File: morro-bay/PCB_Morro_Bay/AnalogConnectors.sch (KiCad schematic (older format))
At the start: 32 parts, among them J10 Conn_01x04, J11 Conn_01x04, J12 Conn_01x04, J13 Conn_01x04, J14 Conn_01x04, J15 Conn_01x04, J16 Conn_01x04, J17 Conn_01x04, J18 Conn_01x04, J19 Conn_01x04, J20 Conn_01x04, J21 Conn_01x04, J22 Conn_01x04, J24 Conn_01x04, J25 Conn_01x04, J26 Conn_01x04, J27 Conn_01x04, J28 Conn_01x04, J29 Conn_01x04, J3 Conn_01x04, J30 Conn_01x04, J31 Conn_01x04, J32 Conn_01x04, J33 Conn_01x04, J34 Conn_01x04, J35 Conn_01x04, J4 Conn_01x04, J5 Conn_01x04, J6 Conn_01x04, J7 Conn_01x04, J8 Conn_01x04, J9 Conn_01x04

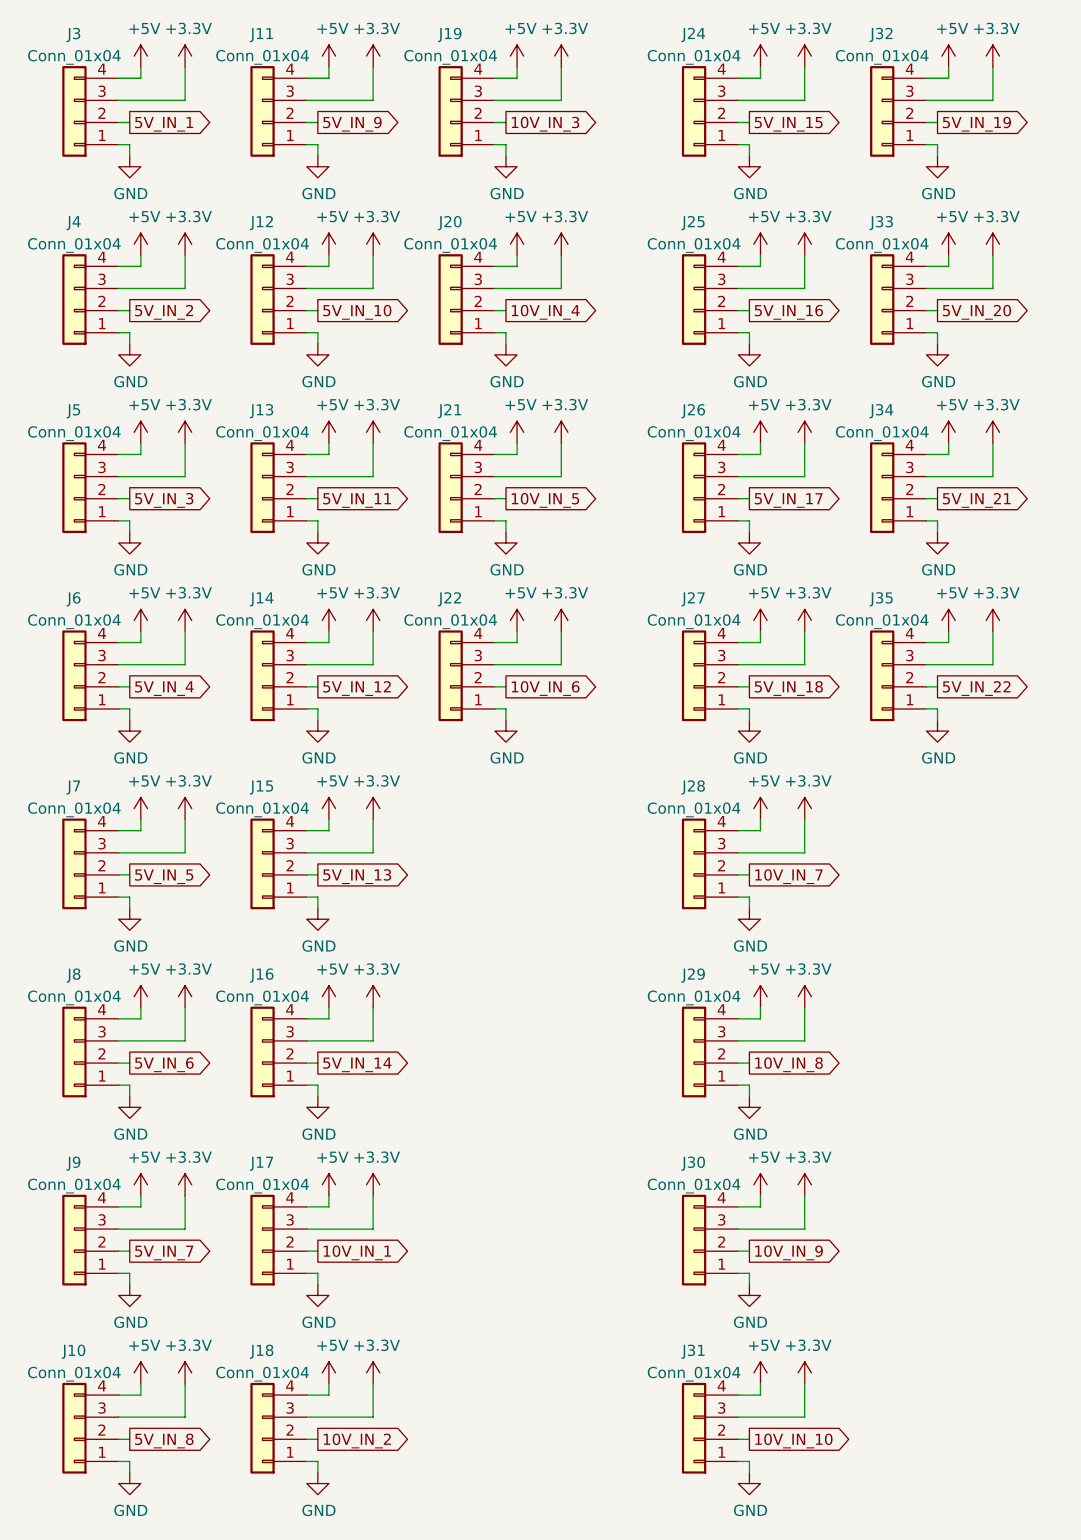
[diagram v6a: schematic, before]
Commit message: Fix values of C7 and C8
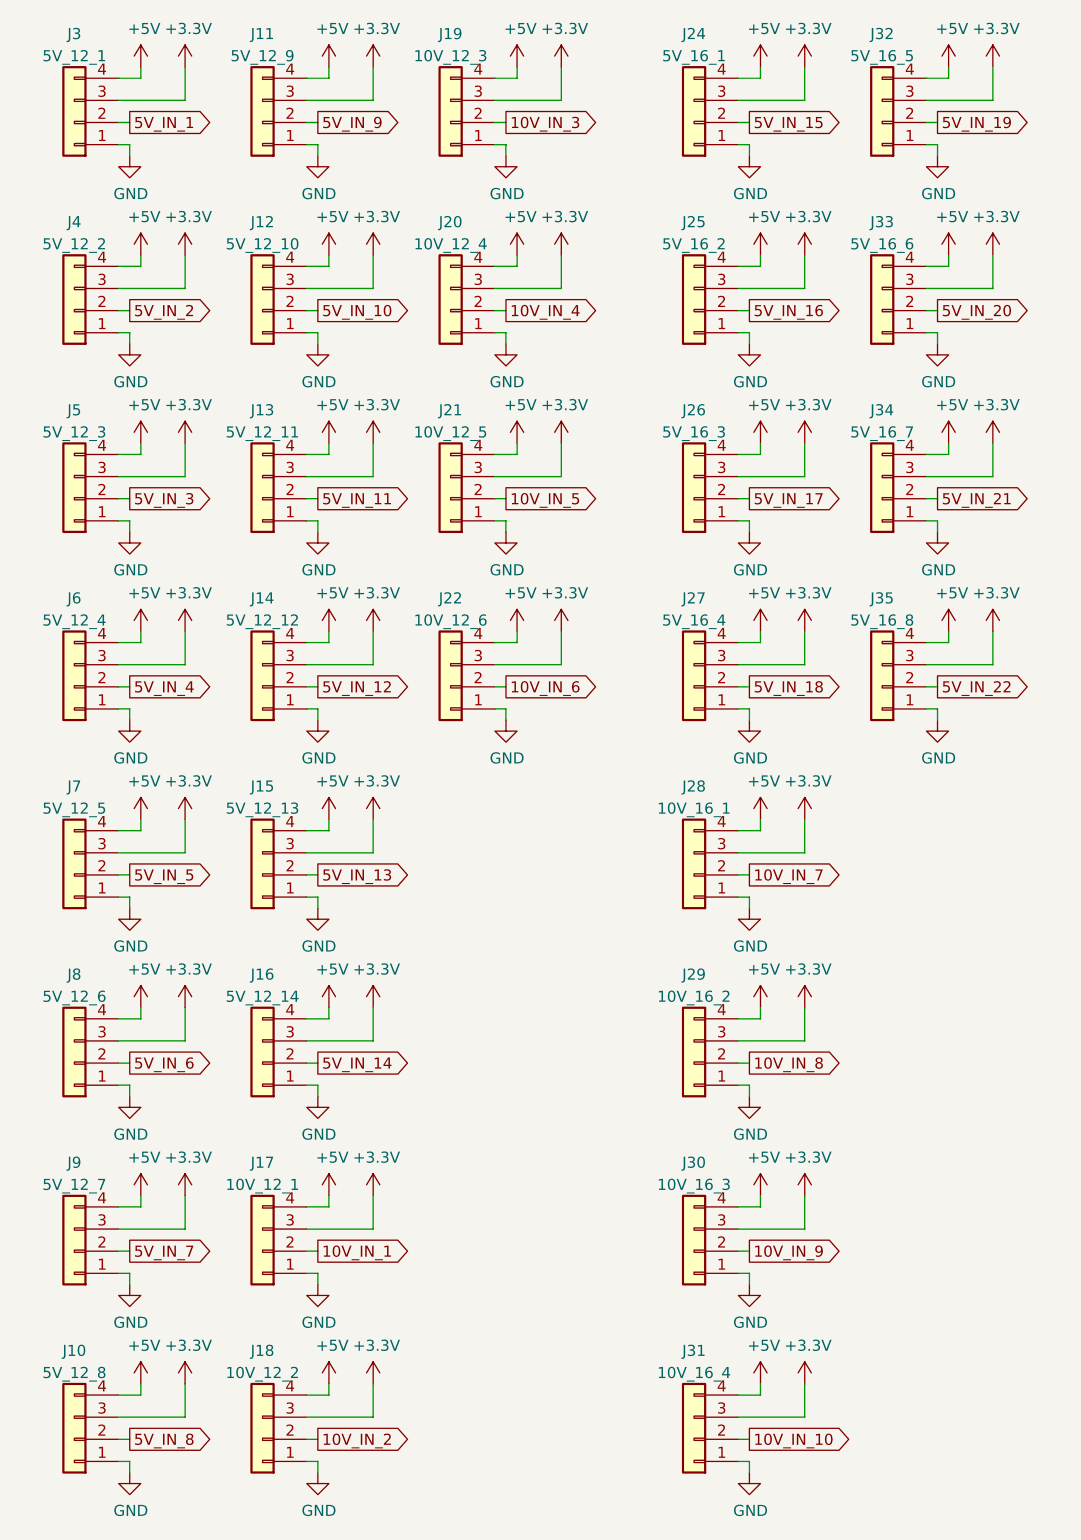
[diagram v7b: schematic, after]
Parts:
- J10: value Conn_01x04 -> 5V_12_8
- J11: value Conn_01x04 -> 5V_12_9
- J12: value Conn_01x04 -> 5V_12_10
- J13: value Conn_01x04 -> 5V_12_11
- J14: value Conn_01x04 -> 5V_12_12
- J15: value Conn_01x04 -> 5V_12_13
- J16: value Conn_01x04 -> 5V_12_14
- J17: value Conn_01x04 -> 10V_12_1
- J18: value Conn_01x04 -> 10V_12_2
- J19: value Conn_01x04 -> 10V_12_3
- J20: value Conn_01x04 -> 10V_12_4
- J21: value Conn_01x04 -> 10V_12_5
- J22: value Conn_01x04 -> 10V_12_6
- J24: value Conn_01x04 -> 5V_16_1
- J25: value Conn_01x04 -> 5V_16_2
- J26: value Conn_01x04 -> 5V_16_3
- J27: value Conn_01x04 -> 5V_16_4
- J28: value Conn_01x04 -> 10V_16_1
- J29: value Conn_01x04 -> 10V_16_2
- J3: value Conn_01x04 -> 5V_12_1
- J30: value Conn_01x04 -> 10V_16_3
- J31: value Conn_01x04 -> 10V_16_4
- J32: value Conn_01x04 -> 5V_16_5
- J33: value Conn_01x04 -> 5V_16_6
- J34: value Conn_01x04 -> 5V_16_7
- J35: value Conn_01x04 -> 5V_16_8
- J4: value Conn_01x04 -> 5V_12_2
- J5: value Conn_01x04 -> 5V_12_3
- J6: value Conn_01x04 -> 5V_12_4
- J7: value Conn_01x04 -> 5V_12_5
- J8: value Conn_01x04 -> 5V_12_6
- J9: value Conn_01x04 -> 5V_12_7

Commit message: More routing
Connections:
- net 10V_IN_10: now also J35.2 (Pin_2); no longer J31.2 (Pin_2)
- net 10V_IN_7: now also J32.2 (Pin_2); no longer J28.2 (Pin_2)
- net 10V_IN_8: now also J33.2 (Pin_2); no longer J29.2 (Pin_2)
- net 10V_IN_9: now also J34.2 (Pin_2); no longer J30.2 (Pin_2)
- net 5V_IN_19: now also J28.2 (Pin_2); no longer J32.2 (Pin_2)
- net 5V_IN_20: now also J29.2 (Pin_2); no longer J33.2 (Pin_2)
- net 5V_IN_21: now also J30.2 (Pin_2); no longer J34.2 (Pin_2)
- net 5V_IN_22: now also J31.2 (Pin_2); no longer J35.2 (Pin_2)
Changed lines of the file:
@@
 Text GLabel 1850 5300 2    50   Output ~ 0
 5V_IN_14
-Text GLabel 3800 4450 2    50   Output ~ 0
+Text GLabel 4650 1050 2    50   Output ~ 0
 10V_IN_7
-Text GLabel 3800 5300 2    50   Output ~ 0
+Text GLabel 4650 1900 2    50   Output ~ 0
 10V_IN_8
-Text GLabel 3800 6150 2    50   Output ~ 0
+Text GLabel 4650 2750 2    50   Output ~ 0
 10V_IN_9
-Text GLabel 3800 7000 2    50   Output ~ 0
+Text GLabel 4650 3600 2    50   Output ~ 0
 10V_IN_10
 Wire Wire Line
@@
 Wire Wire Line
 	4600 1050 4650 1050
-Text GLabel 4650 1050 2    50   Output ~ 0
+Text GLabel 3800 4450 2    50   Output ~ 0
 5V_IN_19
 Wire Wire Line
@@
 Wire Wire Line
 	4600 1900 4650 1900
-Text GLabel 4650 1900 2    50   Output ~ 0
+Text GLabel 3800 5300 2    50   Output ~ 0
 5V_IN_20
 Wire Wire Line
@@
 Wire Wire Line
 	4600 2750 4650 2750
-Text GLabel 4650 2750 2    50   Output ~ 0
+Text GLabel 3800 6150 2    50   Output ~ 0
 5V_IN_21
 Wire Wire Line
@@
 Wire Wire Line
 	4600 3600 4650 3600
-Text GLabel 4650 3600 2    50   Output ~ 0
+Text GLabel 3800 7000 2    50   Output ~ 0
 5V_IN_22
 $EndSCHEMATC
